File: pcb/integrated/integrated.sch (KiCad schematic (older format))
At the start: 4 parts, among them J1001 mounting-hole-grounded, J1002 mounting-hole-grounded, J1003 mounting-hole-grounded, J1004 mounting-hole-grounded

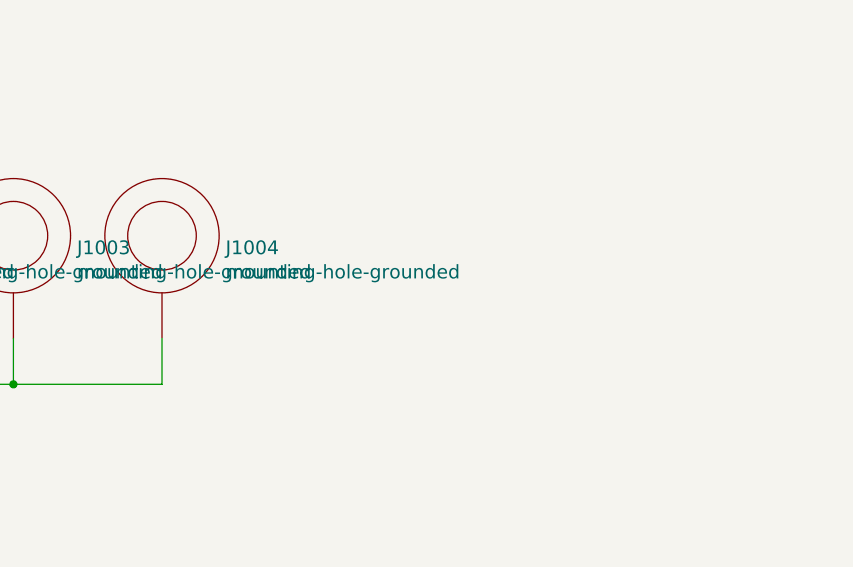
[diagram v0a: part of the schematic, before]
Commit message: schematic fixes and component placement
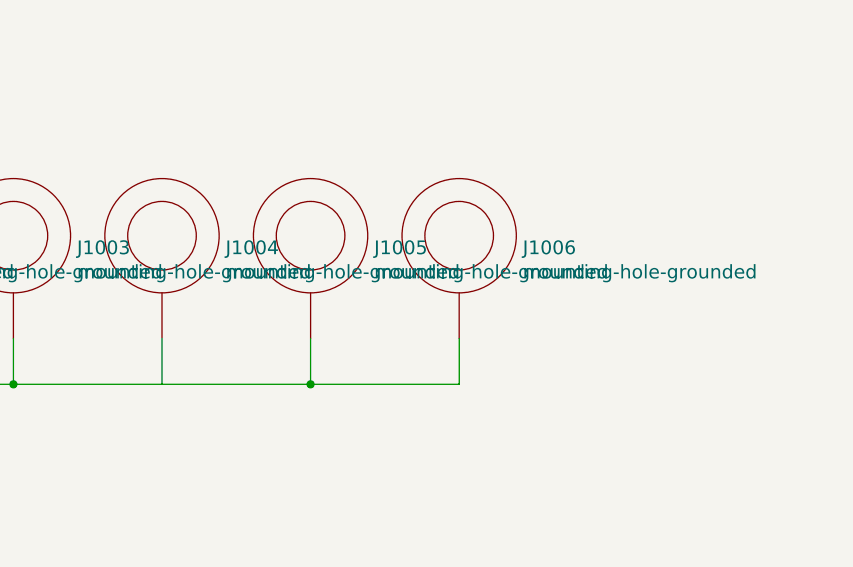
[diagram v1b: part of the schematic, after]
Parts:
- added J1005, J1006: mounting-hole-grounded, wbraun_smd:M3-tight-fit-pan-head, symbol wbraun_ic_lib:mounting-hole-grounded
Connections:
- net Earth: now also J1005.1, J1006.1
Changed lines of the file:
@@
 	1    0    0    -1
 $EndComp
+$Comp
+L wbraun_ic_lib:mounting-hole-grounded J1005
+U 1 1 5D8938B4
+P 7900 2100
+F 0 "J1005" H 8178 2047 60  0000 L CNN
+F 1 "mounting-hole-grounded" H 8178 1941 60  0000 L CNN
+F 2 "wbraun_smd:M3-tight-fit-pan-head" H 7900 2100 60  0001 C CNN
+F 3 "" H 7900 2100 60  0001 C CNN
+	1    7900 2100
+	1    0    0    -1
+$EndComp
+$Comp
+L wbraun_ic_lib:mounting-hole-grounded J1006
+U 1 1 5D8938BA
+P 8550 2100
+F 0 "J1006" H 8828 2047 60  0000 L CNN
+F 1 "mounting-hole-grounded" H 8828 1941 60  0000 L CNN
+F 2 "wbraun_smd:M3-tight-fit-pan-head" H 8550 2100 60  0001 C CNN
+F 3 "" H 8550 2100 60  0001 C CNN
+	1    8550 2100
+	1    0    0    -1
+$EndComp
+Wire Wire Line
+	8550 2750 8550 2550
+Wire Wire Line
+	7900 2550 7900 2750
+Connection ~ 7900 2750
+Wire Wire Line
+	7900 2750 8550 2750
+Wire Wire Line
+	7250 2750 7900 2750
 $EndSCHEMATC

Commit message: PCB routing finihsed, ready for design review
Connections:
- wire segments 12 -> 10
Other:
- moved on the sheet: J1001, J1003
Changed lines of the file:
@@
 L wbraun_ic_lib:mounting-hole-grounded J1001
 U 1 1 5D77E7D7
-P 5300 2100
-F 0 "J1001" H 5578 2047 60  0000 L CNN
-F 1 "mounting-hole-grounded" H 5578 1941 60  0000 L CNN
-F 2 "wbraun_smd:M3-tight-fit-pan-head" H 5300 2100 60  0001 C CNN
-F 3 "" H 5300 2100 60  0001 C CNN
-	1    5300 2100
+P 6900 3600
+F 0 "J1001" H 7178 3547 60  0000 L CNN
+F 1 "mounting-hole-grounded" H 7178 3441 60  0000 L CNN
+F 2 "wbraun_smd:M3-tight-fit-pan-head" H 6900 3600 60  0001 C CNN
+F 3 "" H 6900 3600 60  0001 C CNN
+	1    6900 3600
 	1    0    0    -1
 $EndComp
@@
 L wbraun_ic_lib:mounting-hole-grounded J1003
 U 1 1 5D77E922
-P 6600 2100
-F 0 "J1003" H 6878 2047 60  0000 L CNN
-F 1 "mounting-hole-grounded" H 6878 1941 60  0000 L CNN
-F 2 "wbraun_smd:M3-tight-fit-pan-head" H 6600 2100 60  0001 C CNN
-F 3 "" H 6600 2100 60  0001 C CNN
-	1    6600 2100
+P 8450 3050
+F 0 "J1003" H 8728 2997 60  0000 L CNN
+F 1 "mounting-hole-grounded" H 8728 2891 60  0000 L CNN
+F 2 "wbraun_smd:M3-tight-fit-pan-head" H 8450 3050 60  0001 C CNN
+F 3 "" H 8450 3050 60  0001 C CNN
+	1    8450 3050
 	1    0    0    -1
 $EndComp
@@
 $EndComp
 Wire Wire Line
-	8550 2750 8550 2550
-Wire Wire Line
 	7900 2550 7900 2750
-Connection ~ 7900 2750
-Wire Wire Line
-	7900 2750 8550 2750
 Wire Wire Line
 	7250 2750 7900 2750
